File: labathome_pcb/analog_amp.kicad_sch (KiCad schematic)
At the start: 43 parts, among them J13 SPK, J19 SPK, J22 AudioJack3_SwitchT, J24 AOUT, U10 LM358, U18 MD8002A, U25 NS4168, U5 UDA1334

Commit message: Updated PCB: nRF24l01, SIM7080, LoRa module
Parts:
- C49: footprint Capacitor_SMD:C_0603_1608Metric -> Capacitor_SMD:C_0402_1005Metric
- R48, R50: footprint Resistor_SMD:R_0603_1608Metric -> Resistor_SMD:R_0402_1005Metric
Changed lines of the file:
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@@
     (property "Reference" "R50" (id 0) (at 231.14 100.33 90))
     (property "Value" "k1" (id 1) (at 231.14 102.87 90))
-    (property "Footprint" "Resistor_SMD:R_0603_1608Metric" (id 2) (at 231.14 104.648 90)
+    (property "Footprint" "Resistor_SMD:R_0402_1005Metric" (id 2) (at 231.14 104.648 90)
       (effects (font (size 1.27 1.27)) hide)
     )
@@
       (effects (font (size 1.27 1.27)) hide)
     )
+    (pin "1")
+    (pin "2")
+    (pin "3")
+    (pin "5")
+    (pin "6")
+    (pin "7")
     (pin "4")
     (pin "8")
@@
       (effects (font (size 1.27 1.27)) (justify right))
     )
-    (property "Footprint" "Capacitor_SMD:C_0603_1608Metric" (id 2) (at 235.2548 102.87 0)
+    (property "Footprint" "Capacitor_SMD:C_0402_1005Metric" (id 2) (at 235.2548 102.87 0)
       (effects (font (size 1.27 1.27)) hide)
     )
@@
     (property "Reference" "R48" (id 0) (at 227.33 106.68 90))
     (property "Value" "M22" (id 1) (at 224.79 106.68 90))
-    (property "Footprint" "Resistor_SMD:R_0603_1608Metric" (id 2) (at 226.568 106.68 90)
+    (property "Footprint" "Resistor_SMD:R_0402_1005Metric" (id 2) (at 226.568 106.68 90)
       (effects (font (size 1.27 1.27)) hide)
     )
@@
     (pin "2")
     (pin "3")
+    (pin "5")
+    (pin "6")
+    (pin "7")
+    (pin "4")
+    (pin "8")
   )
   (symbol (lib_id "Device:R") (at 54.61 140.97 90) (unit 1)
@@
       (effects (font (size 1.27 1.27)) hide)
     )
+    (pin "1")
+    (pin "2")
+    (pin "3")
     (pin "5")
     (pin "6")
     (pin "7")
+    (pin "4")
+    (pin "8")
   )
   (symbol (lib_id "power:PWR_FLAG") (at 219.71 72.39 0) (unit 1)

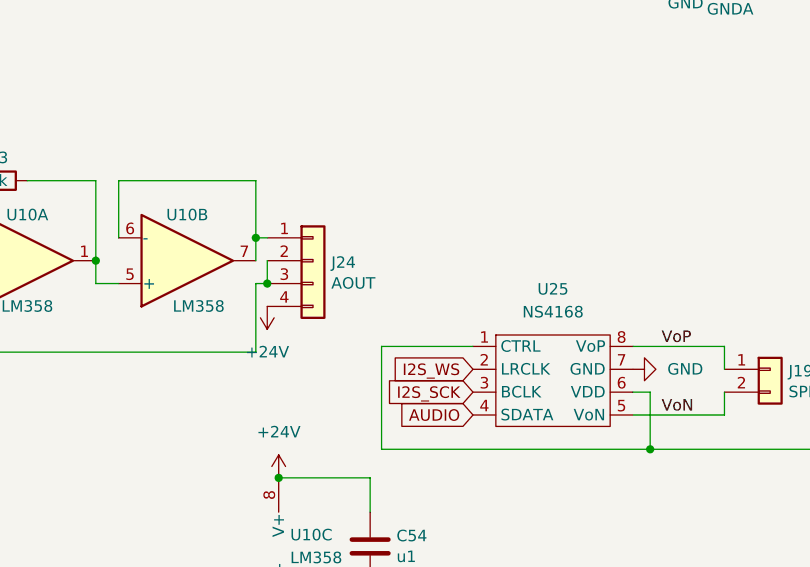
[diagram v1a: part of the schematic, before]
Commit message: LTSpice Simulation & minor optical fixes
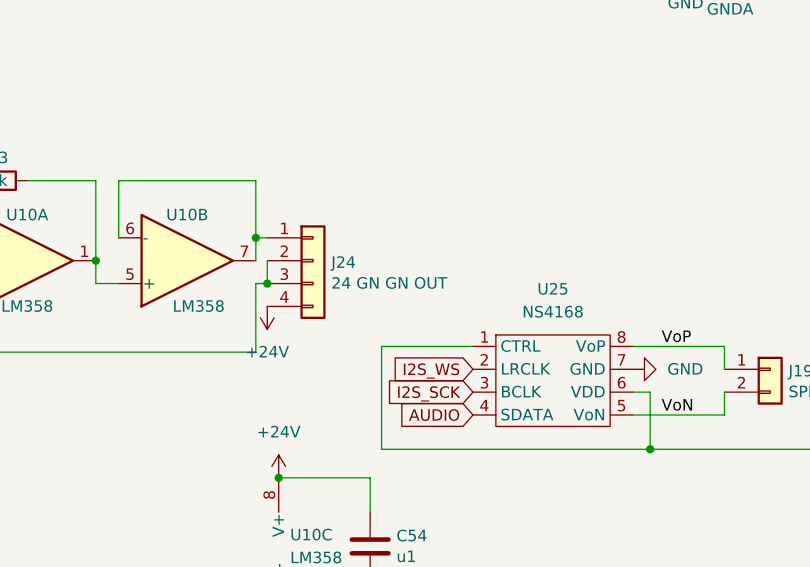
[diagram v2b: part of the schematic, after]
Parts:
- J24: value AOUT -> 24 GN GN OUT
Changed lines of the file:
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@@
       (effects (font (size 1.27 1.27)) (justify left))
     )
-    (property "Value" "AOUT" (id 1) (at 99.822 152.3746 0)
+    (property "Value" "24 GN GN OUT" (id 1) (at 99.822 152.3746 0)
       (effects (font (size 1.27 1.27)) (justify left))
     )
